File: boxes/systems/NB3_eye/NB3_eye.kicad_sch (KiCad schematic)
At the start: 2 parts, among them J1 2x5_Pin_Header_side, J3 Socket_1x5_side

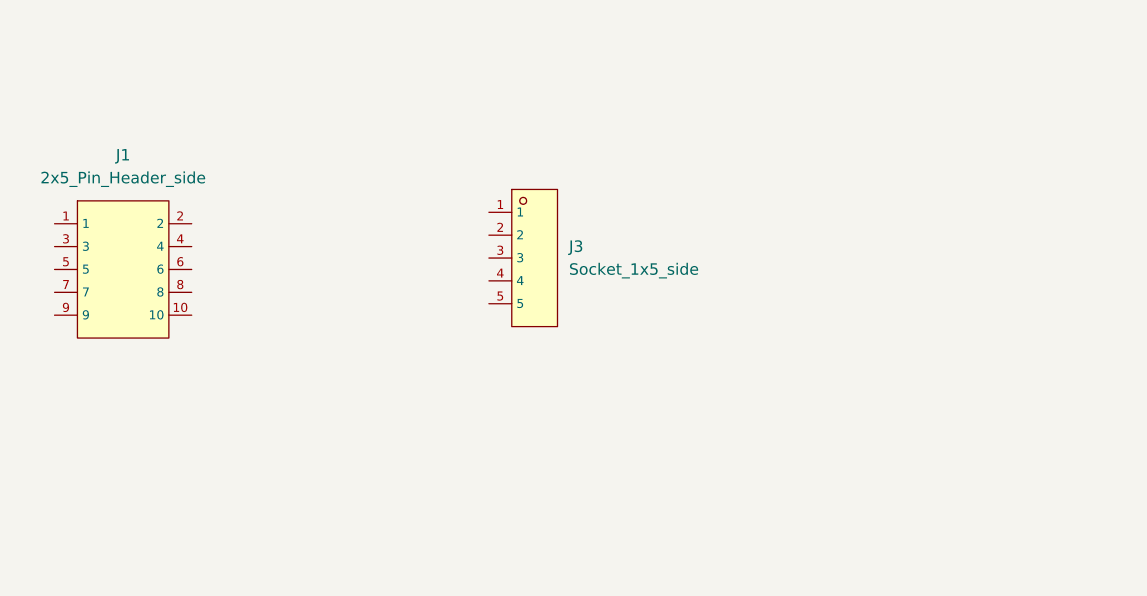
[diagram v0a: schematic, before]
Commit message: Update fabrication details for NB3 eye
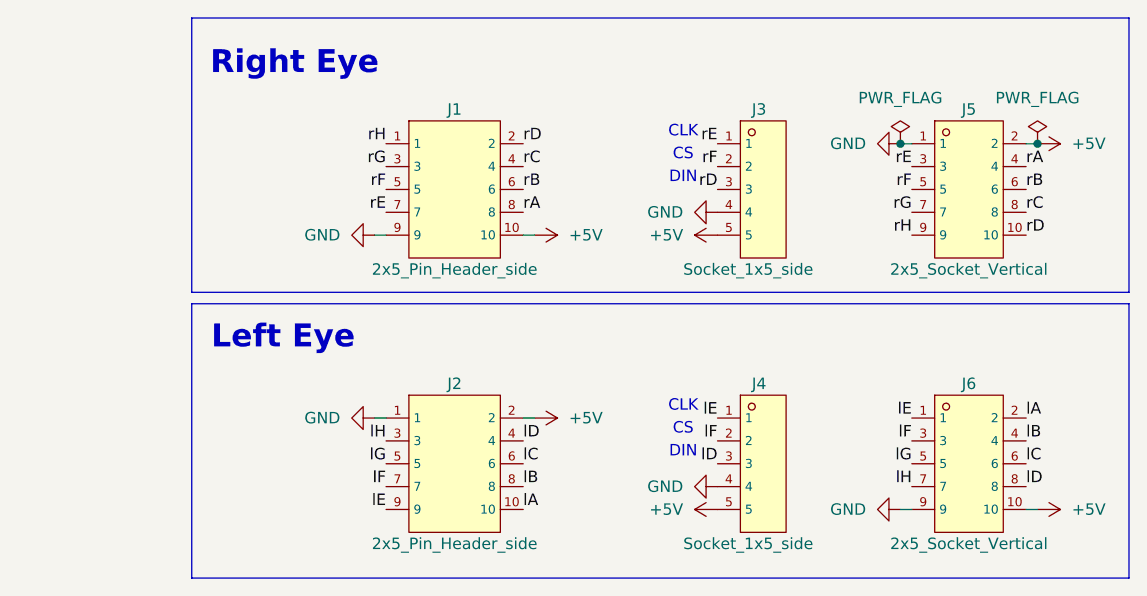
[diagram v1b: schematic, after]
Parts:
- added J2: 2x5_Pin_Header_side, NB3_eye:PinHeader_Male_TH_Side_2x5_C60563, symbol NB3_eye:PinHeader_Male_TH_Side_2x5_C60563
- added J4: Socket_1x5_side, NB3_eye:SocketHeader_Female_TH_Side_1x5_C2897387, symbol NB3_eye:SocketHeader_Female_TH_Side_1x5_C2897387
- added J5, J6: 2x5_Socket_Vertical, NB3_eye:SocketHeader_Female_TH_2x5_C492399, symbol NB3_eye:SocketHeader_Female_TH_2x5_C492399
- J1: footprint PinHeader_Male_TH_Side_2x5_C60563 -> NB3_eye:PinHeader_Male_TH_Side_2x5_C60563
- J3: footprint SocketHeader_Female_TH_Side_1x5_C2897387 -> NB3_eye:SocketHeader_Female_TH_Side_1x5_C2897387
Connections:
- net rH: now reaches J1.1
- net rH: now also J5.9
- net +5V: now reaches J1.10
- net +5V: now also J3.5, J2.2, J4.5, J5.2, J6.10
- net rD: now reaches J1.2
- net rD: now also J3.3, J5.10
- net rG: now reaches J1.3
- net rG: now also J5.7
- net rC: now reaches J1.4
- net rC: now also J5.8
- net rF: now reaches J1.5
- net rF: now also J3.2, J5.5
- net rB: now reaches J1.6
- net rB: now also J5.6
- net rE: now reaches J1.7
- net rE: now also J3.1, J5.3
- net rA: now reaches J1.8
- net rA: now also J5.4
- net GND: now reaches J1.9
- net GND: now also J3.4, J2.1, J4.4, J5.1, J6.9
- new net lA: J2.10, J6.2
- new net lB: J2.8, J6.4
- new net lC: J2.6, J6.6
- new net lD: J2.4, J4.3, J6.8
- new net lE: J2.9, J4.1, J6.1
- new net lF: J2.7, J4.2, J6.3
- new net lG: J2.5, J6.5
- new net lH: J2.3, J6.7
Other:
- note added: "CLK"
- note added: "CS"
- note added: "DIN"
- note added: "Left Eye"
- note added: "Right Eye"
- company: (none) -> Voight-Kampff
- title: (none) -> NB3 Eye Adapter
